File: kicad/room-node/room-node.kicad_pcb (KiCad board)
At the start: 4 copper layers, 89.5 x 38 mm, 57 parts, among them J1 USB4085-GF-A, J2 Speaker 8Ω, J3 Waveshare e-paper, J4 LED strip, SW1 TL3342 RESET, SW2 TL3342 BOOT, U1 ESP32-S3-WROOM-1-N16R8, U2 AP7361C-33ER-13, U3 MAX98357AETE+, U5 USBLC6-2SC6, U6 AHT20

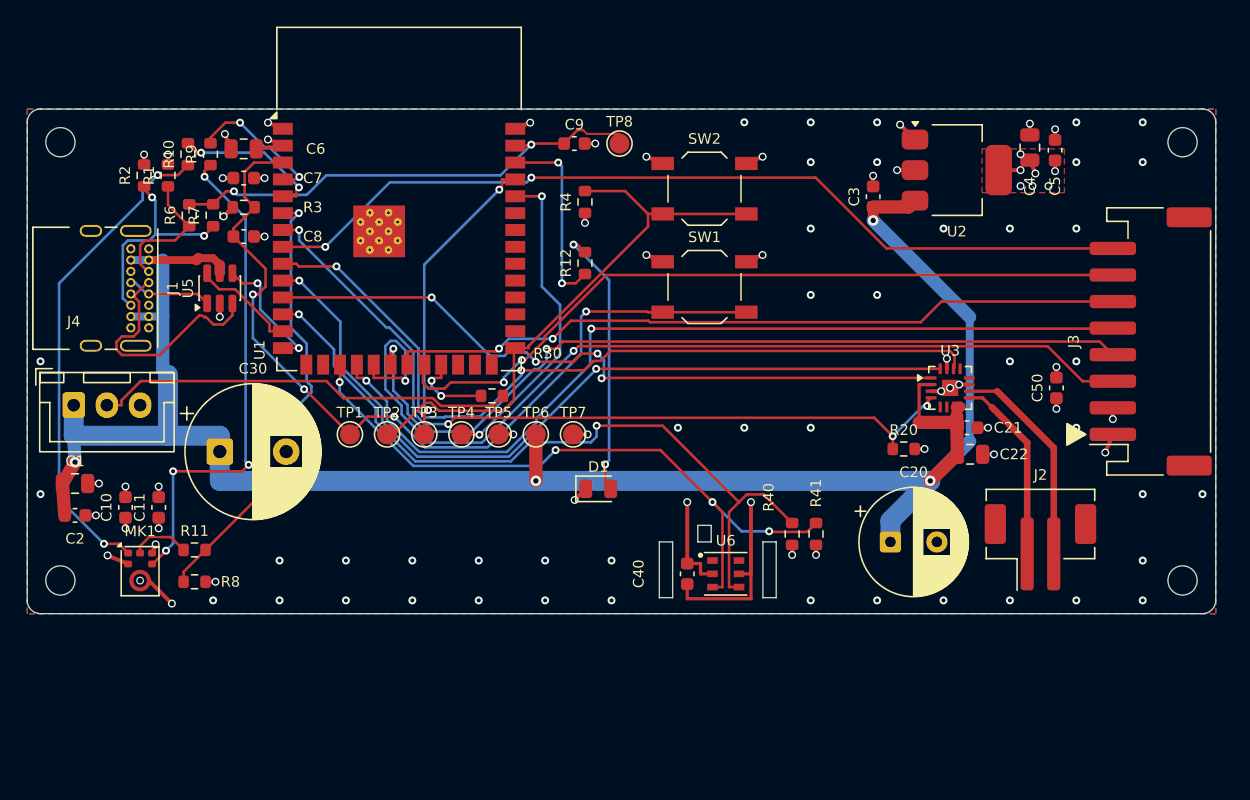
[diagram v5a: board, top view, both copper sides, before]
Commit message: SQU-38: PR #23 review fixes — J3 edge margin, +5V inlet, M3 via drills
Iris's SQU-37 re-review of PR #23 asked for three geometry fixes and a set
of record corrections. Freerouting needs Java 25, which is not in the
container, so the board could not be rebuilt end to end: the three edits are
applied by the coordinate-exact tools/pcb_squ38.py and the same geometry is
now in the generator, so the next full rebuild reproduces it.

1. J3 edge margin. J3 (184.600 -> 184.500, 117.500) rot 90. Mounting-tab
   copper 189.200 -> 189.100 against the routed edge at 189.500: 0.400 mm
   of margin instead of 0.300 mm, which is the DRC limit but not a safe
   milling margin at JLCPCB's +/-0.20 mm routing tolerance. The housing
   front stays 0.55 mm inside the edge, so the cable still leaves straight
   out of the right edge. The pin-1 silk triangle moved with the footprint,
   tip now (179.60, 124.50), 0.30 mm off pin 1's pad. EPD routes are
   unchanged: the pads are 3.5 mm long and the tracks land well inside them.

2. +5V inlet. The common section from J1's VBUS pads to the trunk split
   carries LED + amp + LDO together (3.4 A simultaneous worst case) and was
   1.00 mm for 8.23 mm plus a 0.56 mm turn. It is now one 1.50 mm riser at
   x = 110.60, y 111.375 -> 124.600 (13.23 mm), fed by two 0.60 mm x 1.45 mm
   necks out of the pin field, which is all the 0.70 mm pads on a 0.85 mm
   pitch leave. The necks are in parallel and are the only narrow part;
   the "1.50 mm end to end" claim is corrected in docs/pcb/layout.md.
   Clearance 0.345 mm to J1's A-row pads, 0.200 mm at the necks (unchanged).

3. M3 tab vias. The four 0.30 mm drills are back (0.60 mm pads) with the
   fifth at 0.40 mm — the geometry reviewed in SQU-31. They had come back at
   0.40 mm from the DSN/SES round trip, so route() now calls fix_tab_vias()
   to re-assert them after the import.

4. Records. docs/pcb/layout.md now carries the measured EPD lengths
   (55.76-71.91 mm; EPD_MOSI 71.91 mm / 2 vias, EPD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
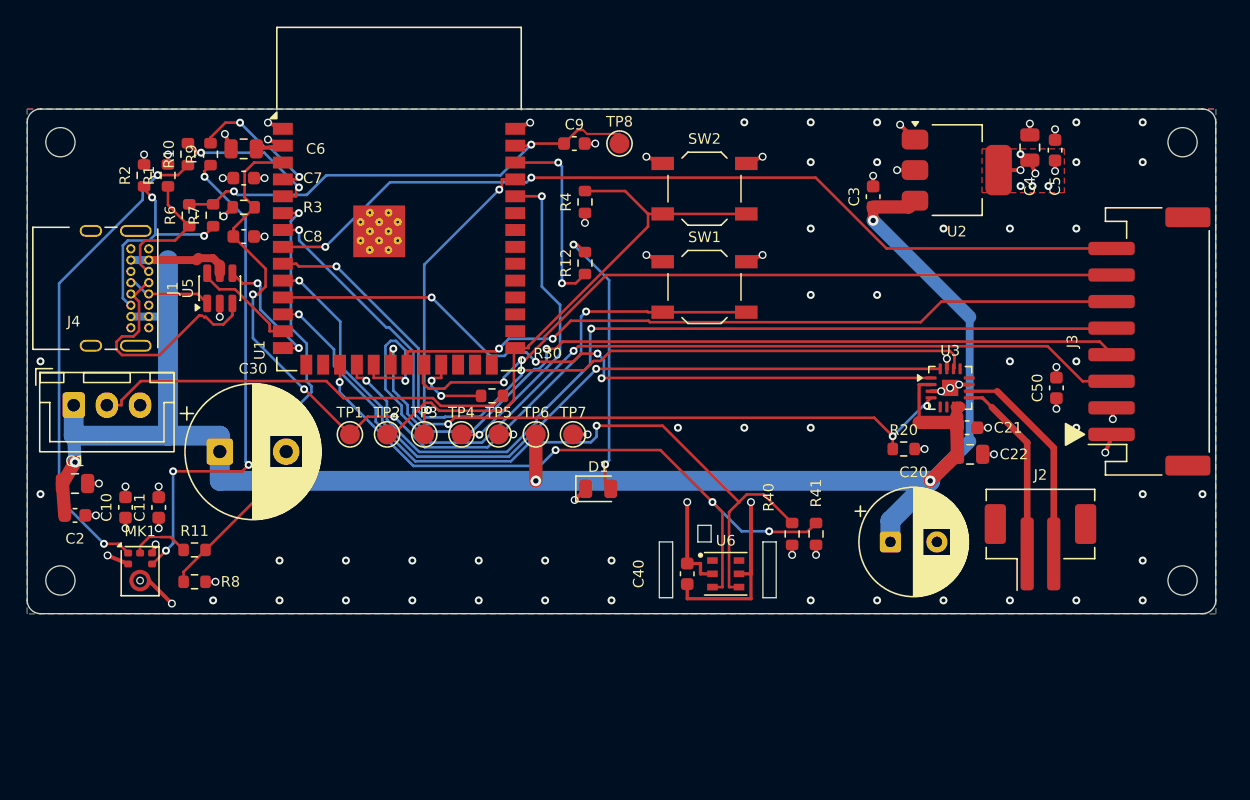
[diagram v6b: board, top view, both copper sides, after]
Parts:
- moved J3 0.10 mm to (184.5, 117.5)
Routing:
- net +5V: track 152.9 -> 153.5 mm
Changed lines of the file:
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@@
 	(footprint "Connector_JST:JST_PH_S8B-PH-SM4-TB_1x08-1MP_P2.00mm_Horizontal"
 		(layer "F.Cu")
-		(at 184.6 117.5 90)
+		(at 184.5 117.5 90)
 		(descr "JST PH series connector, S8B-PH-SM4-TB (http://www.jst-mfg.com/product/pdf/eng/ePH.pdf)")
 		(tags "connector JST PH horizontal")
@@
 	(gr_poly
 		(pts
-			(xy 179.7 124.5) (xy 178.299999 123.7) (xy 178.299999 125.3)
+			(xy 179.6 124.5) (xy 178.199999 123.7) (xy 178.199999 125.3)
 		)
 		(stroke
@@
 		(at 175.7 105.8)
 		(size 0.6)
-		(drill 0.4)
+		(drill 0.3)
 		(layers "F.Cu" "B.Cu")
 		(net "+3V3")
@@
 		(at 174.8 105.8)
 		(size 0.6)
-		(drill 0.4)
+		(drill 0.3)
 		(layers "F.Cu" "B.Cu")
 		(net "+3V3")
@@
 		(at 174.8 103.4)
 		(size 0.6)
-		(drill 0.4)
+		(drill 0.3)
 		(layers "F.Cu" "B.Cu")
 		(net "+3V3")
@@
 		(at 176.9 105.8)
 		(size 0.6)
-		(drill 0.4)
+		(drill 0.3)
 		(layers "F.Cu" "B.Cu")
 		(net "+3V3")
@@
 	)
 	(segment
+		(start 110.6 111.375)
+		(end 110.6 115.625)
+		(width 1.5)
+		(layer "B.Cu")
+		(net "+5V")
+	)
+	(segment
 		(start 110.6 124.6)
 		(end 103.5 124.6)
@@
 	)
 	(segment
-		(start 110.205 119.6)
-		(end 110.6 120)
-		(width 1)
+		(start 110.6 115.625)
+		(end 110.6 124.6)
+		(width 1.5)
 		(layer "B.Cu")
 		(net "+5V")
 	)
 	(segment
-		(start 103.5 124.6)
-		(end 103.6 126.6)
-		(width 1)
+		(start 109.155 115.625)
+		(end 110.6 115.625)
+		(width 0.6)
 		(layer "B.Cu")
 		(net "+5V")
 	)
 	(segment
-		(start 163.7 108.3918)
-		(end 170.9686 115.6604)
+		(start 103.5 124.6)
+		(end 103.6 126.6)
 		(width 1)
 		(layer "B.Cu")
@@
 	)
 	(segment
-		(start 110.205 111.375)
-		(end 110.205 115.625)
+		(start 163.7 108.3918)
+		(end 170.9686 115.6604)
 		(width 1)
 		(layer "B.Cu")
@@
 	)
 	(segment
-		(start 110.205 115.625)
-		(end 109.155 115.625)
-		(width 0.6)
-		(layer "B.Cu")
-		(net "+5V")
-	)
-	(segment
 		(start 165 131)
 		(end 165 132.6)
@@
 	)
 	(segment
-		(start 109.155 111.375)
-		(end 110.205 111.375)
-		(width 0.6)
-		(layer "B.Cu")
-		(net "+5V")
-	)
-	(segment
 		(start 109.155 115.625)
 		(end 107.805 115.625)
@@
 	)
 	(segment
-		(start 110.205 115.625)
-		(end 110.205 119.6)
-		(width 1)
-		(layer "B.Cu")
-		(net "+5V")
-	)
-	(segment
 		(start 170.9686 125.0314)
 		(end 168 128)
@@
 	)
 	(segment
-		(start 110.6 120)
-		(end 110.6 124.6)
-		(width 1.5)
-		(layer "B.Cu")
-		(net "+5V")
-	)
-	(segment
 		(start 114.5 128)
 		(end 168 128)
@@
 		(layer "B.Cu")
 		(net "+5V")
+	)
+	(segment
+		(start 109.155 111.375)
+		(end 110.6 111.375)
+		(width 0.6)
+		(layer "B.Cu")
+		(net "+5V")

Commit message: SQU-39: centre USB-C, LED connector to the bottom edge left of the AHT20
- J1 centred on the left edge (pin field and courtyard centre y = 119.000); U5 moves
  with it. C1/C2 under U5 on the +5V spine via.
- J4 to the bottom edge under U1 (124.0, 133.6): 18.81 mm courtyard to U6, 15.60 mm
  to the island slot. C30 at J4, + pad facing pin 1 (6.16 mm).
- +5V: 1.50 mm riser -> spine at y = 124.0 (5.85 mm above the island box, was 1.85)
  -> C30 -> J4. J1 -> J4 26.08 mm, 2.1 C rise at 1.6 A (IPC-2221).
- J1 -> U5 USB pair hand-routed; U5 -> U1 forced to F.Cu. D+/D- now 11.5/12.4 mm
  (A) and 13.1/14.0 mm (B), ~1 mm skew (was 15.5 mm).
- TP1-TP7 + D1 in one row under U1; mic passives re-spread, fixed label spots.
- Full pipeline re-run (Freerouting 2.4.1 / Temurin 25); reports and Gerbers
  regenerated; layout.md updated. DRC 0 err / 0 unconnected / 0 parity, ERC 0 err,
  check_pinout PASS, 12 silk warnings (was 14).

Co-Authored-By: Claude Opus 5.5 <noreply@anthropic.com>
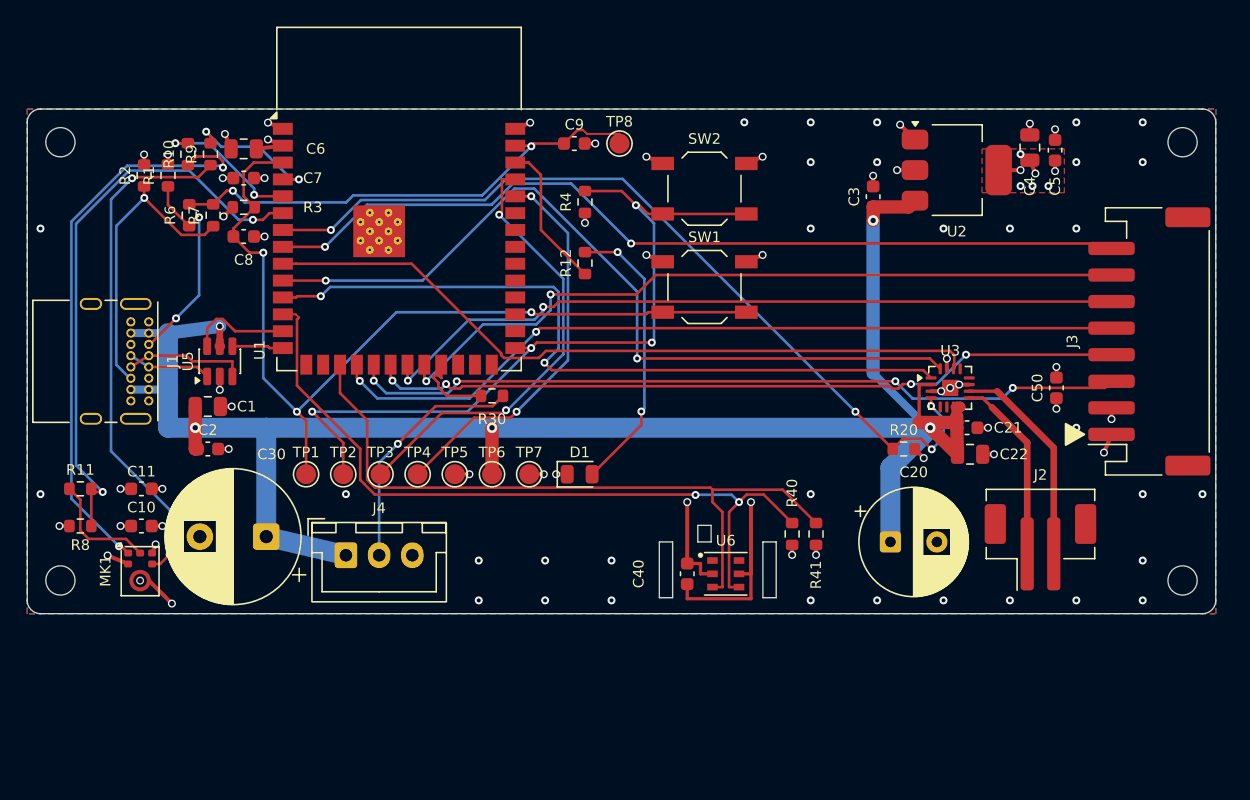
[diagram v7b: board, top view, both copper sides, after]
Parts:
- moved J4 23.4 mm to (124.0, 133.6)
- moved C1 11.6 mm to (113.6, 122.4)
- moved C2 11.2 mm to (113.6, 125.6)
- moved R11 9.75 mm to (104.0, 128.6)
- moved R8 9.57 mm to (104.0, 131.4), turned to 180 degrees
- moved C30 7.29 mm to (118.0, 132.2), turned to 180 degrees
- moved J1 5.50 mm to (109.2, 116.0)
- moved U5 5.50 mm to (114.5, 119.0)
- moved TP3 4.46 mm to (126.6, 127.5)
- moved TP5 4.46 mm to (132.2, 127.5)
- moved TP6 4.46 mm to (135.0, 127.5)
- moved TP1 4.46 mm to (121.0, 127.5)
- moved TP2 4.46 mm to (123.8, 127.5)
- moved TP4 4.46 mm to (129.4, 127.5)
- moved TP7 4.46 mm to (137.8, 127.5)
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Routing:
- net IO0: track 42.8 -> 58.4 mm, vias 0 -> 4
- net Net-(J4-Pin_2): track 31.9 -> 18.4 mm, vias 0 -> 1
- net EPD_MOSI: track 71.9 -> 58.7 mm, vias 2 -> 4
- net +5V: track 153.5 -> 142.5 mm, vias 4 -> 5
- net TXD0: track 22.9 -> 33.8 mm
- net I2S_MIC_DATA: track 33.8 -> 43.8 mm
- net USB_D+_CONN: track 18.9 -> 9.20 mm
- net EPD_CLK: track 64.1 -> 57.1 mm, vias 2 -> 4
- net Net-(MK1-WS): track 36.9 -> 43.6 mm
- net I2S_SPK_LRCLK: track 61.6 -> 55.0 mm, vias 2 -> 0
- net CC2: track 16.3 -> 22.4 mm, vias 2 -> 1
- net EPD_CS: track 66.6 -> 60.7 mm
- net USB_D+: track 9.58 -> 3.86 mm, vias 2 -> 0
- net CC1: track 10.2 -> 15.9 mm, vias 0 -> 2
- net RXD0: track 24.4 -> 29.6 mm
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
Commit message: SQU-42: J4 LED connector to side entry (S3B-XH-A), cable out of the bottom edge
- J4 footprint JST_XH_B3B-XH-A vertical -> JST_XH_S3B-XH-A_1x03_P2.50mm_Horizontal
  (JST S3B-XH-A(LF)(SN), LCSC C157928, 3 A), mouth facing the bottom edge.
  Pins at (124.0/126.5/129.0, 128.45); housing front 0.30 mm inside the edge, no
  body overhang; silk 0.18 mm off the edge. Pin order unchanged (1 +5V, 2 DIN, 3 GND).
- J4 courtyard -> U6 courtyard 18.81 mm, -> island slot 15.60 mm (unchanged).
  C30 stays at J4 (courtyards 0.21 mm, C30+ -> pin 1 7.08 mm).
- TP1-TP7 + D1 into a 2 x 4 block right of J4 (the housing covers the old row);
  TP6 (+5V) still drops straight onto the spine.
- Full pipeline re-run (Freerouting 2.4.1 / Temurin 25); Gerbers, renders, DRC/ERC
  reports and schematic PDF regenerated. BOM, schematic.md, layout.md updated.
  DRC 0 errors / 0 unconnected / 0 parity (12 silk warnings, same set as main),
  ERC 0 errors (1 known warning), check_pinout PASS.

Co-Authored-By: Claude Opus 5.5 <noreply@anthropic.com>
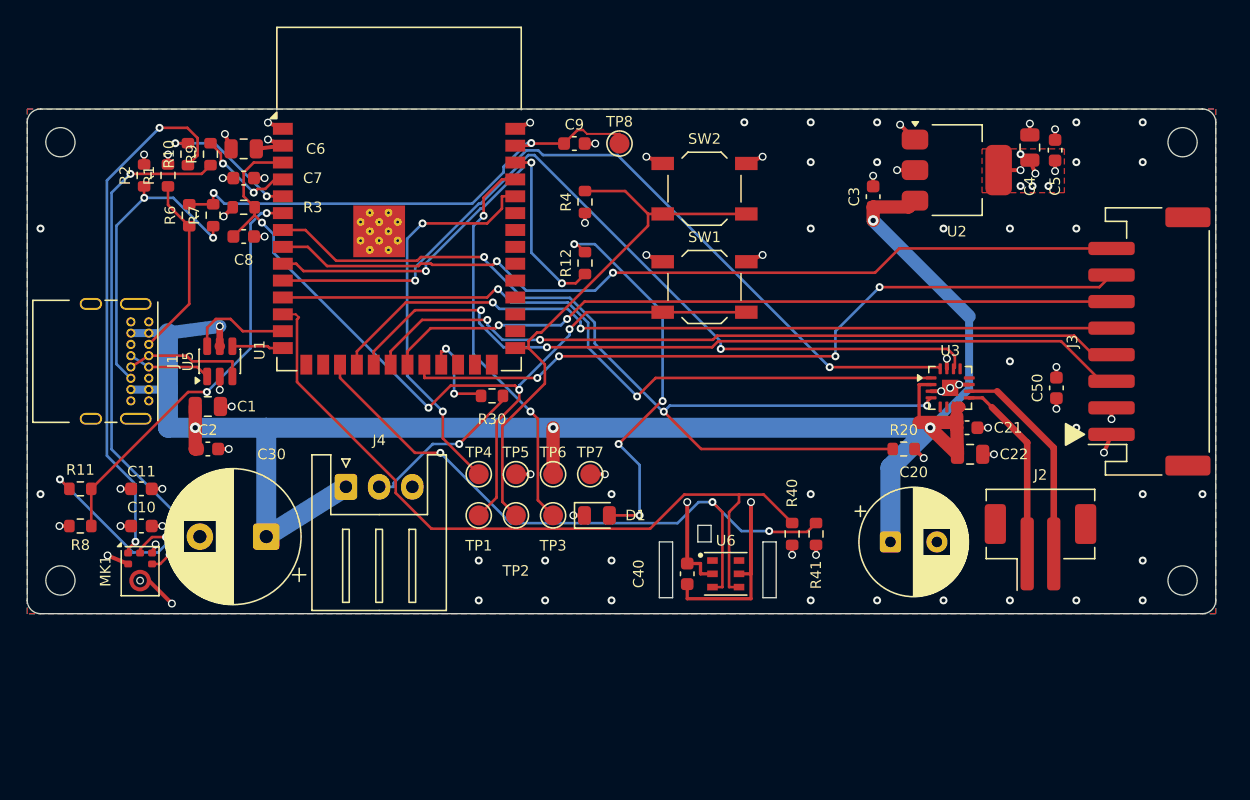
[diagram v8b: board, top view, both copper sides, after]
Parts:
- J4: footprint Connector_JST:JST_XH_B3B-XH-A_1x03_P2.50mm_Vertical -> Connector_JST:JST_XH_S3B-XH-A_1x03_P2.50mm_Horizontal
- moved TP2 13.4 mm to (136.8, 130.6)
- moved TP1 13.4 mm to (134.0, 130.6)
- moved TP3 13.4 mm to (139.6, 130.6)
- moved J4 5.15 mm to (124.0, 128.4)
- moved TP5 4.60 mm to (136.8, 127.5)
- moved TP4 4.60 mm to (134.0, 127.5)
- moved TP6 4.60 mm to (139.6, 127.5)
- moved TP7 4.60 mm to (142.4, 127.5)
- moved D1 3.36 mm to (142.9, 130.6)
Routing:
- net IO0: track 58.4 -> 42.7 mm, vias 4 -> 0
- net I2S_MIC_DATA: track 43.8 -> 31.3 mm
- net AMP_SD: track 64.2 -> 74.7 mm, vias 4 -> 3
- net Net-(D1-A): track 21.7 -> 29.5 mm, vias 2 -> 4
- net I2S_SPK_LRCLK: track 55.0 -> 62.7 mm, vias 0 -> 2
- net Net-(MK1-DATA): track 8.69 -> 14.7 mm, vias 0 -> 2
- net Net-(J4-Pin_2): track 18.4 -> 12.5 mm
- net TXD0: track 33.8 -> 29.7 mm
- net Net-(MK1-WS): track 43.6 -> 40.3 mm
- net +5V: track 142.5 -> 145.7 mm
- net I2S_MIC_BCLK: track 10.7 -> 7.75 mm
- net I2S_SPK_DIN: track 56.6 -> 54.1 mm
- net EPD_MOSI: track 58.7 -> 61.2 mm, vias 4 -> 2
- net I2C_SCL: track 53.1 -> 50.7 mm, vias 0 -> 3
- net STATUS_LED: track 11.2 -> 13.3 mm, vias 0 -> 2
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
